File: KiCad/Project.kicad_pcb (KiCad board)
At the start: 2 copper layers, 0 parts

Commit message: started working on blaster PCB
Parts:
- added BT1: 7.4V, AlexWheelockFootprintLibrary:Project_Battery_Connector, F.Cu at (150.5, 88.9)
- added C1: 220uF, AlexWheelockFootprintLibrary:Project_16V_220uF_Capacitor, F.Cu at (148.1, 108.6)
- added C2: 0.1uF, Capacitor_SMD:C_0805_2012Metric_Pad1.18x1.45mm_HandSolder, F.Cu at (35.1, 33.8)
- added C3: 220uF, AlexWheelockFootprintLibrary:Project_16V_220uF_Capacitor, F.Cu at (151.9, 115.3)
- added C4: 0.1uF, Capacitor_SMD:C_0805_2012Metric_Pad1.18x1.45mm_HandSolder, F.Cu at (35.1, 36.8)
- added C6: 1uF, Capacitor_SMD:C_0805_2012Metric_Pad1.18x1.45mm_HandSolder, F.Cu at (21.7, 74.9)
- added C7: 1uF, Capacitor_SMD:C_0805_2012Metric_Pad1.18x1.45mm_HandSolder, F.Cu at (3.98, 56.1)
- added C8: 50pF, Capacitor_SMD:C_0805_2012Metric_Pad1.18x1.45mm_HandSolder, F.Cu at (35.0, 72.2)
- added D1: 1N4148, Diode_SMD:D_0805_2012Metric_Pad1.15x1.40mm_HandSolder, F.Cu at (51.2, 46.5)
- added D2: +5V, LED_SMD:LED_0805_2012Metric_Pad1.15x1.40mm_HandSolder, F.Cu at (44.7, 51.8)
- added D3: +7.4V, LED_SMD:LED_0805_2012Metric_Pad1.15x1.40mm_HandSolder, F.Cu at (44.7, 56.1)
- added D4: 1N4148, Diode_SMD:D_0805_2012Metric_Pad1.15x1.40mm_HandSolder, F.Cu at (3.58, 64.0)
- added D5: 1N4148, Diode_SMD:D_0805_2012Metric_Pad1.15x1.40mm_HandSolder, B.Cu at (74.1, 118.9)
- added J1: ~, Connector_PinHeader_2.54mm:PinHeader_1x05_P2.54mm_Vertical, F.Cu at (94.1, 106.0)
- added J2: Inputs Test Points, Connector_PinHeader_2.54mm:PinHeader_1x05_P2.54mm_Vertical, F.Cu at (108.8, 129.4)
- added J3: Power & Output Test Points, Connector_PinHeader_2.54mm:PinHeader_1x04_P2.54mm_Vertical, F.Cu at (108.8, 125.4)
- added LD1: Laser Diode, AlexWheelockFootprintLibrary:Project_Locking_Output_Header, F.Cu at (102.2, 115.1)
- added Q1: BUK9832-55A, Package_TO_SOT_SMD:SOT-223-3_TabPin2, B.Cu at (75.2, 99.7)
- added Q2: BUK9832-55A, Package_TO_SOT_SMD:SOT-223-3_TabPin2, B.Cu at (75.2, 107.9)
- added R10: 330Ω, Resistor_SMD:R_0805_2012Metric_Pad1.20x1.40mm_HandSolder, F.Cu at (27.5, 76.3)
- added R11: 330Ω, Resistor_SMD:R_0805_2012Metric_Pad1.20x1.40mm_HandSolder, F.Cu at (27.6, 80.7)
- added R12: 330Ω, Resistor_SMD:R_0805_2012Metric_Pad1.20x1.40mm_HandSolder, F.Cu at (27.6, 83.7)
- added R13: 1kΩ, Resistor_SMD:R_1206_3216Metric_Pad1.30x1.75mm_HandSolder, B.Cu at (66.8, 118.0)
- added R14: 100kΩ, Resistor_SMD:R_0805_2012Metric_Pad1.20x1.40mm_HandSolder, B.Cu at (54.3, 103.5)
- added R15: 0Ω, Resistor_SMD:R_0805_2012Metric_Pad1.20x1.40mm_HandSolder, B.Cu at (59.7, 109.9)
- added R2: 4.7kΩ, Resistor_SMD:R_0805_2012Metric_Pad1.20x1.40mm_HandSolder, F.Cu at (35.0, 39.8)
- added R3: 8.2kΩ, Resistor_SMD:R_0805_2012Metric_Pad1.20x1.40mm_HandSolder, F.Cu at (35.0, 42.7)
- added R5: 10kΩ, Resistor_SMD:R_0805_2012Metric_Pad1.20x1.40mm_HandSolder, F.Cu at (-5.07, 57.1)
- added R6: 100kΩ, Resistor_SMD:R_0805_2012Metric_Pad1.20x1.40mm_HandSolder, B.Cu at (59.1, 96.6)
- added R7: 0Ω, Resistor_SMD:R_0805_2012Metric_Pad1.20x1.40mm_HandSolder, B.Cu at (59.9, 101.8)
- added R8: 330Ω, Resistor_SMD:R_0805_2012Metric_Pad1.20x1.40mm_HandSolder, F.Cu at (27.5, 70.4)
- added R9: 330Ω, Resistor_SMD:R_0805_2012Metric_Pad1.20x1.40mm_HandSolder, F.Cu at (27.5, 73.3)
- added S1: Solenoid, AlexWheelockFootprintLibrary:Project_Locking_Output_Header, F.Cu at (133.1, 115.1)
- added SW1: Power, AlexWheelockFootprintLibrary:Project_Locking_Output_Header, F.Cu at (143.4, 115.1)
- added SW2: Fire, AlexWheelockFootprintLibrary:Project_Locking_Output_Header, F.Cu at (126.4, 115.1)
- added SW3: Freq Select, AlexWheelockFootprintLibrary:Project_Blaster_Freq_Switch, F.Cu at (140.8, 87.2)
- added SW4: Fire Select, AlexWheelockFootprintLibrary:Project_Blaster_FireSelect_Switch, F.Cu at (160.3, 100.2)
- added U1: TLV1117-50, Package_TO_SOT_SMD:SOT-223-3_TabPin2, F.Cu at (171.7, 82.9)
- added U2: PIC16F1788-IP, AlexWheelockFootprintLibrary:SSOP-28, F.Cu at (136.3, 101.3)
- added U3: Audio Board, AlexWheelockFootprintLibrary:Project_Audio_Board, F.Cu at (99.8, 110.6)
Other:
- board outline added: 79.2 x 30.5 mm

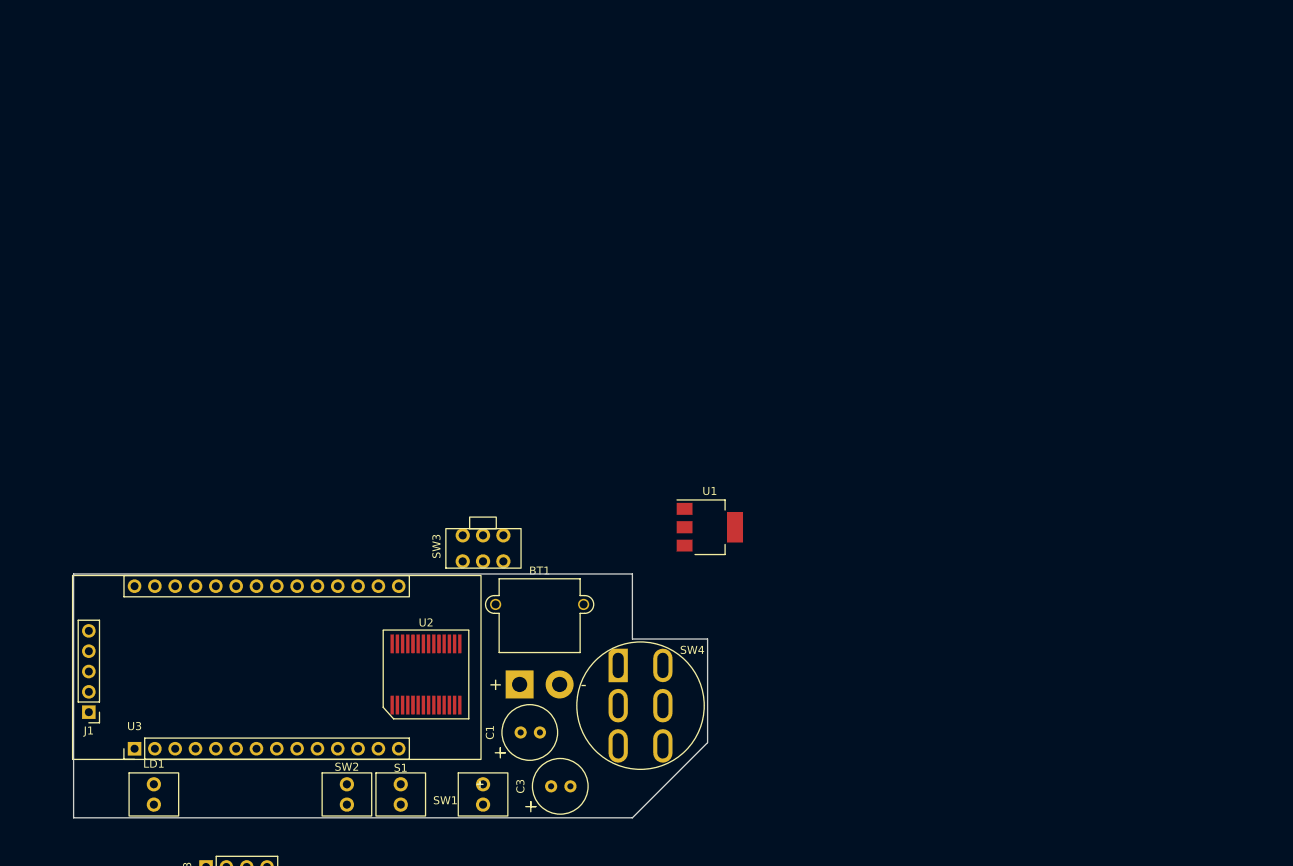
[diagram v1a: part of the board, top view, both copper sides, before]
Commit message: working on the PCB for the blaster
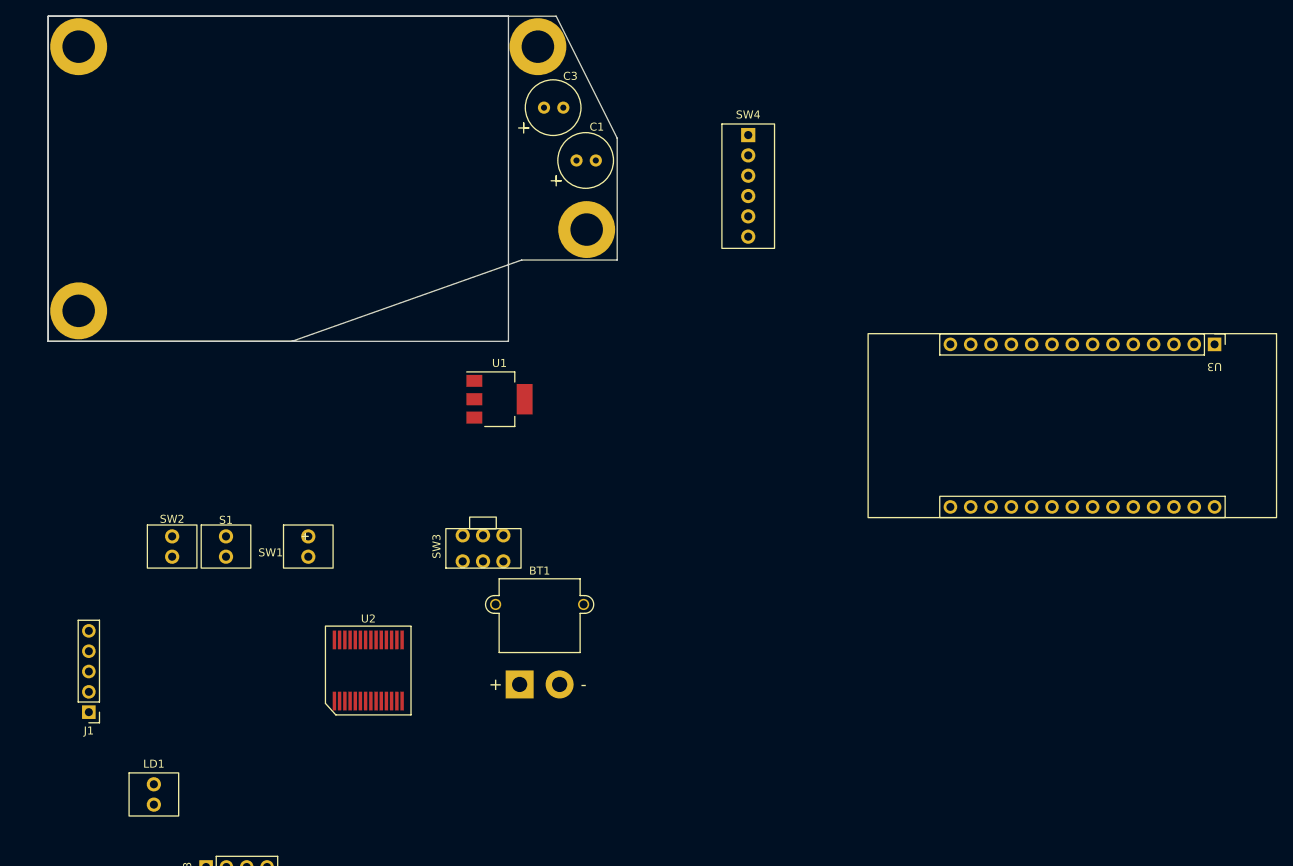
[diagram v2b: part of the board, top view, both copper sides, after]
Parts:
- added ?: , , F.Cu at (92.8, 55.9)
- added ?: , , F.Cu at (92.8, 22.9)
- added ?: , , F.Cu at (150.2, 22.9)
- added REF**: 6-32 Mount, AlexWheelockFootprintLibrary:6-32 Mount, F.Cu at (156.3, 45.7)
- SW4: footprint AlexWheelockFootprintLibrary:Project_Blaster_FireSelect_Switch -> AlexWheelockFootprintLibrary:Project_Locking_Header_1x06
- moved U3 144.2 mm to (234.8, 60.1), turned to -90 degrees
- moved C3 84.8 mm to (151.0, 30.5)
- moved C1 71.8 mm to (155.1, 37.1)
- moved SW4 68.3 mm to (176.5, 33.9)
- moved S1 37.9 mm to (111.3, 84.1)
- moved SW1 37.9 mm to (121.5, 84.1)
- moved SW2 37.9 mm to (104.5, 84.1)
- moved U1 30.8 mm to (145.4, 66.9)
- moved U2 7.24 mm to (129.0, 100.8)
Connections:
- BT1 pad 1: +7.4V -> Net-(BT1-+)
- S1 pad 1: +7.4V -> Net-(D5-K)
- U1 pad 3: +7.4V -> Net-(D1-K)
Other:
- board size 79.2 x 30.5 mm -> 71.1 x 40.6 mm

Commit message: got a lot done on the blaster PCB
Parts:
- C6, C7, D4, R10, R11, R12, R5, R8, R9: moved to B.Cu
- D5, Q1, Q2, R13, R14, R15, R6, R7: moved to F.Cu
- moved C8 150.7 mm to (185.7, 70.5)
- moved R5 123.4 mm to (118.3, 51.8), turned to -90 degrees
- moved R13 119.1 mm to (176.5, 71.8), turned to -90 degrees
- moved D5 115.8 mm to (179.8, 71.7), turned to -90 degrees
- moved D4 114.0 mm to (116.5, 48.4), turned to 180 degrees
- moved C7 111.6 mm to (115.5, 51.8), turned to -90 degrees
- moved C4 109.2 mm to (143.4, 22.6)
- moved C2 108.4 mm to (143.2, 42.7), turned to 180 degrees
- moved J2 108.3 mm to (112.9, 21.2)
- moved R3 108.1 mm to (143.1, 39.9)
- moved R2 108.1 mm to (143.1, 37.2)
- moved D3 106.3 mm to (149.7, 39.9)
- moved D2 106.1 mm to (149.7, 37.2)
- moved J3 104.5 mm to (100.5, 21.2)
- moved R15 100.1 mm to (135.2, 44.1), turned to 90 degrees
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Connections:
- LD1 pad 2: (no net) -> Net-(LD1-K)
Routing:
- net +5V: track 0.00 -> 77.3 mm
- net Net-(D1-K): track 0.00 -> 45.5 mm
- net Net-(Q2-G): track 0.00 -> 38.8 mm
- net RB7: track 0.00 -> 34.9 mm
- net Net-(Q1-G): track 0.00 -> 29.9 mm
- net Net-(U2-INT/AN12/RB0): track 0.00 -> 10.2 mm
- net Net-(U2-P1D/AN11/RB4): track 0.00 -> 5.36 mm
- net Net-(D4-A): track 0.00 -> 5.19 mm
- net Net-(D5-K): track 0.00 -> 5.00 mm
- net Net-(D3-K): track 0.00 -> 4.59 mm
- net Net-(Q2-D): track 0.00 -> 4.58 mm
- net Net-(D2-K): track 0.00 -> 4.58 mm
- net Net-(SW3-A): track 0.00 -> 4.07 mm
- net Net-(U2-PGM/C12IN2-/AN8/RB3): track 0.00 -> 4.00 mm
- net Net-(U2-VSS-Pad19): track 0.00 -> 3.86 mm
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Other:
- board size 71.1 x 40.6 mm -> 132.9 x 81.5 mm
- board text added: "+5V"
- board text added: "+7.4V"
- board text added: "Burst"
- board text added: "Fire"
- board text added: "Frequency"
- board text added: "Full-Auto"
- board text added: "Laser"
- board text added: "Program"
- board text added: "Semi-Auto"
- board text added: "Solenoid"

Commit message: blaster PCB is nearly finished
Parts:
- added REF**: PinHeader_1x15_P2.54mm_Vertical, Connector_PinHeader_2.54mm:PinHeader_1x15_P2.54mm_Vertical, F.Cu at (98.5, 50.7)
- added REF**: PinHeader_1x11_P2.54mm_Vertical, Connector_PinHeader_2.54mm:PinHeader_1x11_P2.54mm_Vertical, F.Cu at (102.9, 28.2)
- moved SW1 44.7 mm to (189.2, 64.1), turned to -90 degrees
- moved C6 28.3 mm to (98.4, 34.1), turned to -90 degrees
- moved C7 23.8 mm to (101.9, 32.3), turned to 180 degrees
- moved R5 23.4 mm to (101.8, 35.1), turned to 180 degrees
- moved D4 18.8 mm to (105.3, 33.3), turned to 90 degrees
- moved J2 10.1 mm to (123.0, 21.0), turned to -90 degrees
- moved D5 8.23 mm to (171.7, 70.8)
- moved S1 8.03 mm to (171.6, 64.1), turned to 90 degrees
- moved J3 6.98 mm to (107.4, 21.0), turned to -90 degrees
- moved LD1 5.50 mm to (164.2, 64.1)
- moved C8 5.42 mm to (180.5, 68.8)
- moved SW2 5.42 mm to (179.2, 64.1)
- moved BT1 5.01 mm to (201.1, 59.2)
- moved SW3 4.72 mm to (210.6, 65.4)
- moved SW4 3.92 mm to (214.7, 83.1)
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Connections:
- BT1 pad : (no net) -> GND
- C6 pad 1: Net-(C6-Pad1) -> GND
- C7 pad 2: Net-(C7-Pad2) -> GND
- D5 pad 1: Net-(D5-K) -> +7.4V
- J1 pad 3: Net-(J1-Pad3) -> GND
- J2 pad 1: Fire -> Net-(U2-INT/AN12/RB0)
- J2 pad 2: Frequency Select -> Net-(SW3-A)
- J2 pad 3: Full-Auto -> Net-(U2-P1B/AN8/RB2)
- J2 pad 4: Burst -> Net-(U2-PGM/C12IN2-/AN8/RB3)
- J2 pad 5: Semi-Auto -> Net-(U2-P1D/AN11/RB4)
- J3 pad 1: +7.4V -> Net-(D1-K)
- J3 pad 3: Laser/PWM -> Net-(Q2-G)
- J3 pad 4: Solenoid -> Net-(Q1-G)
- R10 pad 2: Net-(R10-Pad2) -> GND
- R11 pad 2: Net-(R10-Pad2) -> GND
- R12 pad 2: Net-(R10-Pad2) -> GND
- R14 pad 2: Net-(R14-Pad2) -> GND
- R15 pad 2: Net-(R15-Pad2) -> GND
- R6 pad 2: Net-(R6-Pad2) -> GND
- R7 pad 2: Net-(R7-Pad2) -> GND
- R8 pad 2: Net-(R10-Pad2) -> GND
- R9 pad 2: Net-(R10-Pad2) -> GND
- S1 pad 1: Net-(D5-K) -> +7.4V
- U3 pad 14: Net-(U3-GND-Pad14) -> GND
- U3 pad 15: Net-(U3-GND-Pad14) -> GND
- U3 pad 18: Net-(U3-GND-Pad14) -> GND
- U3 pad 27: Net-(U3-GND-Pad14) -> GND
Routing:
- net Net-(D4-K): track 3.72 -> 71.3 mm, vias 0 -> 1
- net +5V: track 77.3 -> 143.8 mm, vias 0 -> 1
- net Net-(Q2-G): track 38.8 -> 101.8 mm
- net Net-(U2-P1D/AN11/RB4): track 5.36 -> 66.4 mm
- net Net-(U2-PGM/C12IN2-/AN8/RB3): track 4.00 -> 63.7 mm
- net Net-(U2-P1B/AN8/RB2): track 3.18 -> 61.7 mm
- net Net-(SW3-A): track 4.07 -> 61.2 mm
- net Net-(U2-INT/AN12/RB0): track 10.2 -> 65.3 mm
- net VOL+: track 0.00 -> 39.0 mm
- net RB7: track 34.9 -> 73.3 mm, vias 0 -> 1
- net RB6: track 0.00 -> 37.7 mm
- net Net-(D1-K): track 45.5 -> 77.0 mm, vias 0 -> 1
- net TRIG0: track 0.00 -> 25.3 mm
- net TRIG1: track 0.00 -> 23.5 mm
- net TRIG2: track 0.00 -> 21.9 mm
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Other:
- board size 132.9 x 81.5 mm -> 70 x 40.6 mm
- board text added: "Freq."
- board text added: "Full"
- board text added: "Semi"
- board text added: "Sol."
- board text removed: "Frequency"
- board text removed: "Full-Auto"
- board text removed: "Semi-Auto"
- board text removed: "Solenoid"
